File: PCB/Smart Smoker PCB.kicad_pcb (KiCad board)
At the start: 4 copper layers, 90 x 45 mm, 78 parts, among them J1 105017-0001, J2 393570002, J3 393570002, J4 393570002, J5 393570002, J6 393570002, J7 393570002, J8 Hopper, J9 Lid, Q1 Q_PMOS_GSD, Q2 25V 1.5A Trans, Q3 25V 1.5A Trans, Q4 Q_PMOS_GSD, Q5 2N7002T-7-F, Q6 2N7002T-7-F, U1 ESP32-WROOM-32UE_16MB, U2 DG409LEDY-T1-GE3, U3 MAX31855KASA, U4 AMS1117-3.3, U5 CP2102N-Axx-xQFN28, U6 LTC4412xS6

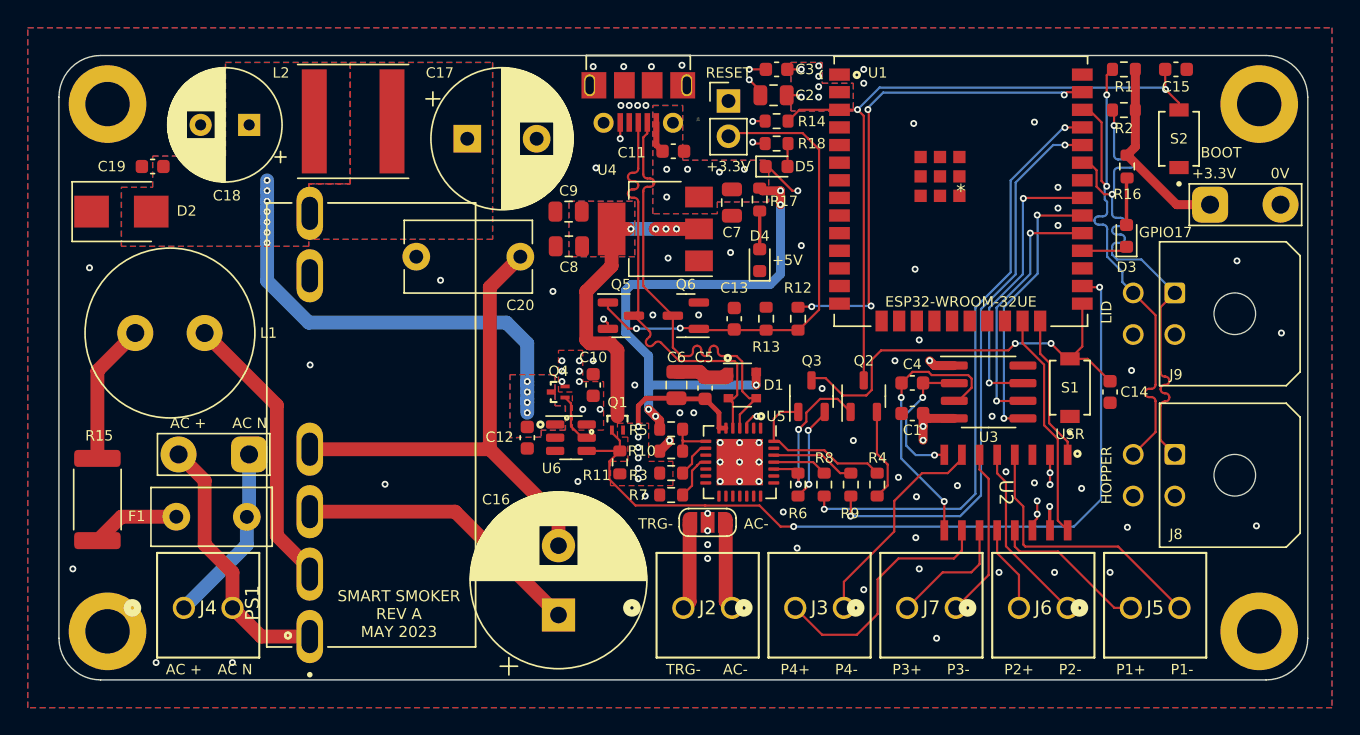
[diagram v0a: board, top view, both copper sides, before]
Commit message: MOV added to PCB1
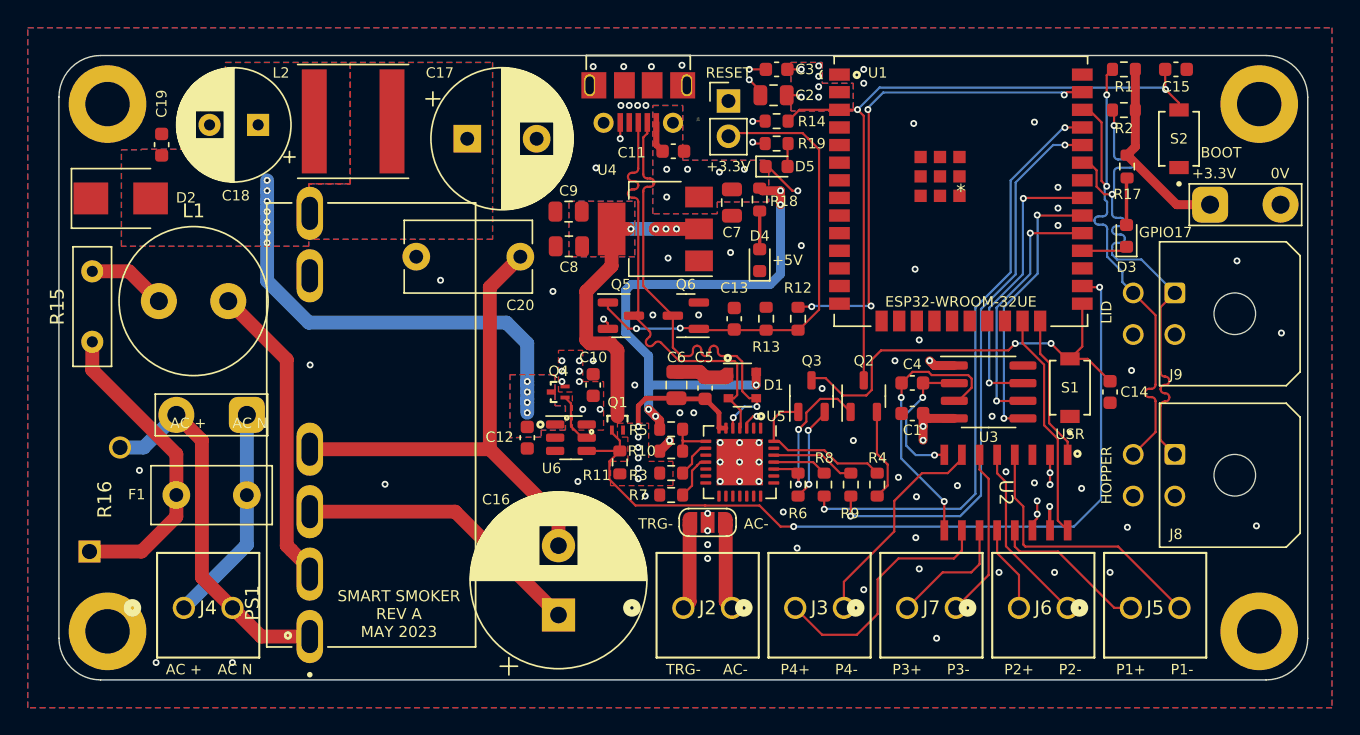
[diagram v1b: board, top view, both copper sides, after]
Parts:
- added R16: B72214S0351K101, Customs Smoker:VARS_B72214S_15P5X5P6-7P5-2P2_TDK, F.Cu at (103.3, 132.0)
- C15: value 1uF 25V X5R 0603 -> 0.1uF 50V X7R 0603
- L1: value 2.2mH 350mA 3.2Ohm TH -> 2.2mH 500mA 2.5Ohm TH; footprint Inductor_THT:L_Radial_D12.0mm_P5.00mm_Fastron_11P -> Inductor_THT:L_Radial_D10.5mm_P5.00mm_Abacron_AISR-01
- R15: footprint Resistor_SMD:R_2512_6332Metric -> Resistor_THT:R_Box_L8.4mm_W2.5mm_P5.08mm
- moved R15 11.4 mm to (102.4, 120.6)
- moved L1 2.86 mm to (107.2, 117.7)
- moved TP1 2.85 mm to (113.5, 125.9)
- moved C19 1.70 mm to (107.4, 106.4), turned to 90 degrees
- moved F1 1.57 mm to (113.5, 131.7)
- moved D2 0.95 mm to (104.5, 110.3)
- moved C18 0.64 mm to (114.4, 105.0)
- renumbered R16 to R17, R17 to R18, R18 to R19
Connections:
- U5 pad 4: /USB_DN -> /USB_DP
- U5 pad 5: /USB_DP -> /USB_DN
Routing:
- net Net-(F1-Pad2): track 6.40 -> 22.4 mm
- net /AC_N: track 19.1 -> 27.0 mm
- net Net-(L1-Pad1): track 10.2 -> 5.69 mm
- net /AC_L: track 13.0 -> 15.8 mm
- net Net-(L1-Pad2): track 20.4 -> 22.0 mm
- net /USB_DN: track 31.5 -> 32.3 mm, vias 0 -> 2
- net GND: vias 84 -> 83

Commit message: 3x PCB ordered
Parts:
- added AE1: Antenna, Symbol:KiCad-Logo2_5mm_SilkScreen, B.Cu at (107.0, 109.4)
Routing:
- net GND: track 17.6 -> 17.1 mm, vias 83 -> 86
